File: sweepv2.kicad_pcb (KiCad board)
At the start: 2 copper layers, 216.9 x 86.6 mm, 50 parts, among them J1 AudioJack4dpb, J2 AudioJack4dpb, SW10 SW_Push, SW11 SW_Push, SW11_r1 SW_Push, SW12 SW_Push, SW12_r1 SW_Push, SW13_r1 SW_Push, SW14 SW_Push, SW15 SW_Push, SW15_r1 SW_Push, SW16 SW_Push, SW16_r1 SW_Push, SW17 SW_Push, SW17_r1 SW_Push, SW18 SW_Push, SW18_r1 SW_Push, SW2 SW_Push, SW20 SW_Push, SW20_r1 SW_Push, SW21 SW_Push, SW21_r1 SW_Push, SW2_r1 SW_Push, SW3 SW_Push, SW3_r1 SW_Push, SW4 SW_Push, SW4_r1 SW_Push, SW5 SW_Push, SW5_r1 SW_Push, SW6 SW_Push, SW6_r1 SW_Push, SW7_r1 SW_Push, SW8 SW_Push, SW8_r1 SW_Push, SW9 SW_Push, SW9_r1 SW_Push, U1 ProMicro-kbd, U2 ProMicro-kbd

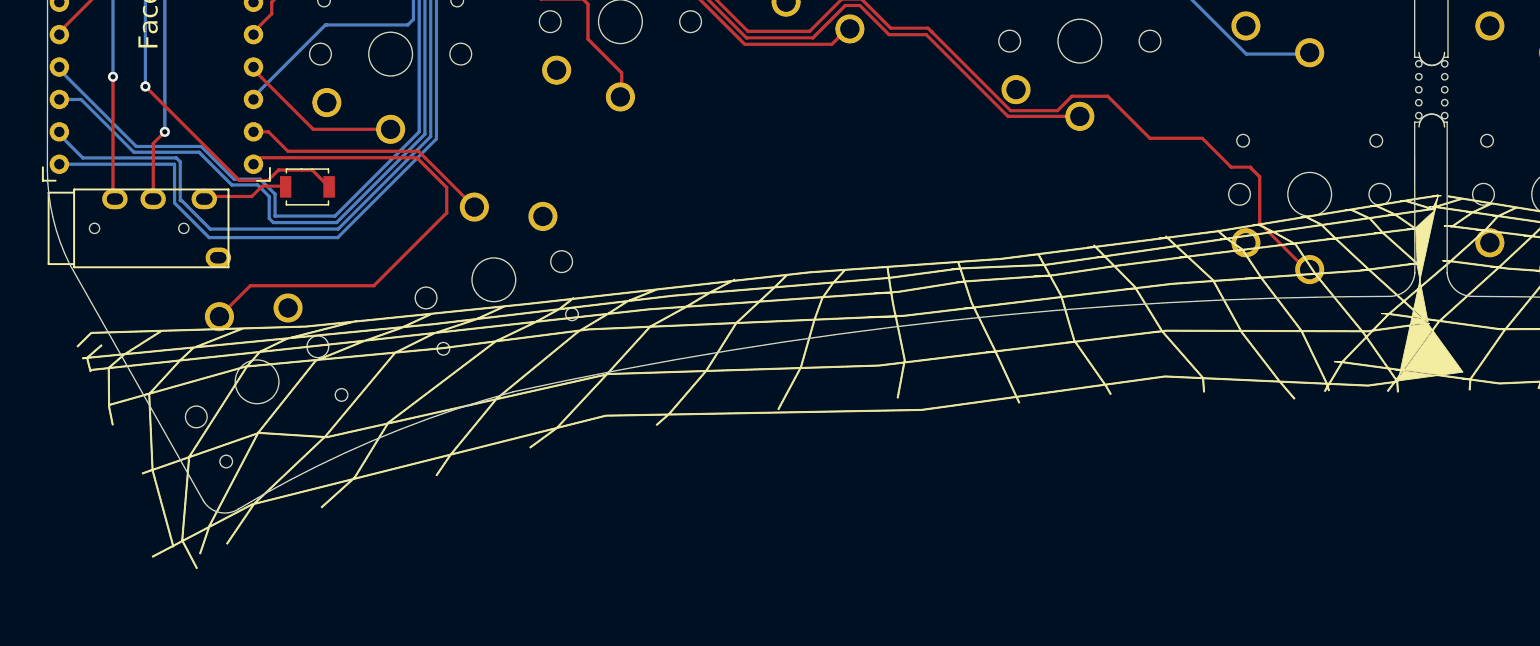
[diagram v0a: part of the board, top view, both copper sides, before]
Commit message: Add basic logos to board
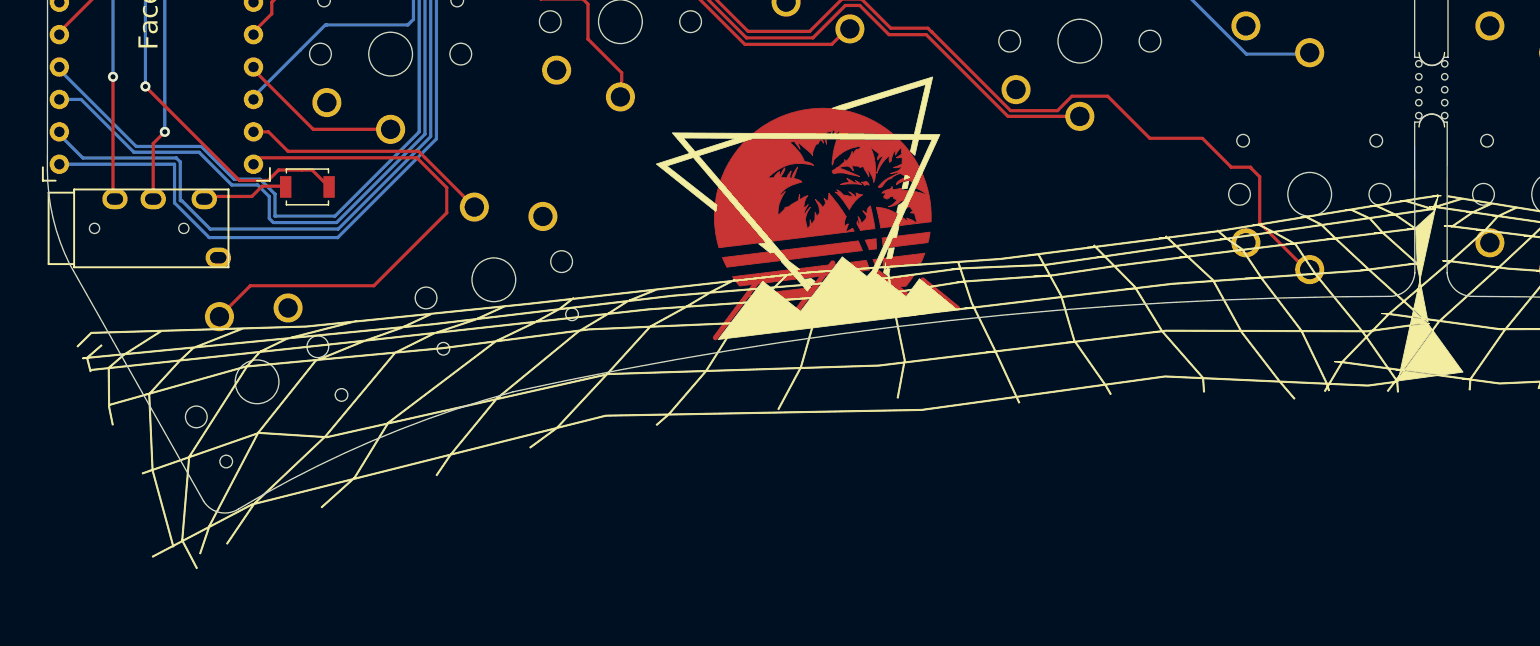
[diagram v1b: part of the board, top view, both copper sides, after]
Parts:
- added G***: LOGO, Kailh:ferris_broom, F.Cu at (82.7, 85.2)
- added G***: LOGO, Library:ferris_broom, F.Cu at (176.3, 83.2)
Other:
- board text removed: "Sweep v 2.2"

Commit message: Remove B logo footprint
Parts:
- removed the G*** at (176.3, 83.2)
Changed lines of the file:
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@@
     )
-  )
-  (footprint "Library:ferris_broom" (layer "F.Cu")
-    (at 176.291396 83.226564)
-    (attr board_only exclude_from_pos_files exclude_from_bom)
-    (fp_text reference "G***" (at 0 0) (layer "F.SilkS") hide
-      (effects (font (size 1.524 1.524) (thickness 0.3)))
-    )
-    (fp_text value "LOGO" (at 0.75 0) (layer "F.SilkS") hide
-      (effects (font (size 1.524 1.524) (thickness 0.3)))
-    )
-    (fp_poly (pts
-        (xy 0.893703 -2.398889)
-        (xy -0.517408 -2.398889)
-        (xy -0.517408 -4.515556)
-        (xy 0.893703 -4.515556)
-      ) (layer "F.Mask") (width 0) (fill solid))
-    (fp_poly (pts
-        (xy 0.893703 2.257777)
-        (xy -0.517408 2.257777)
-        (xy -0.517408 -0.117593)
-        (xy 0.893703 -0.117593)
-      ) (layer "F.Mask") (width 0) (fill solid))
-    (fp_poly (pts
-        (xy 3.786688 -7.190788)
-        (xy 5.46311 -5.844352)
-        (xy 5.446596 -4.374445)
-        (xy 5.430083 -2.904538)
-        (xy 5.324688 -2.516482)
-        (xy 5.289097 -2.385703)
-        (xy 5.257136 -2.268751)
-        (xy 5.231118 -2.174053)
-        (xy 5.213356 -2.110036)
-        (xy 5.206857 -2.087269)
-        (xy 5.205831 -2.062536)
-        (xy 5.228913 -2.050199)
-        (xy 5.286103 -2.046256)
-        (xy 5.309736 -2.046112)
-        (xy 5.425049 -2.046112)
-        (xy 5.440654 -0.405695)
-        (xy 5.443421 -0.100554)
-        (xy 5.446033 0.214915)
-        (xy 5.448444 0.533626)
-        (xy 5.450612 0.848493)
-        (xy 5.452493 1.152429)
-        (xy 5.454044 1.438347)
-        (xy 5.45522 1.699161)
-        (xy 5.455978 1.927785)
-        (xy 5.456275 2.117131)
-        (xy 5.456277 2.132757)
-        (xy 5.456296 3.030792)
-        (xy 4.947144 4.856574)
-        (xy 3.843525 5.950021)
-        (xy 3.63503 6.156573)
-        (xy 3.421343 6.368225)
-        (xy 3.207342 6.58015)
-        (xy 2.997905 6.787519)
-        (xy 2.797908 6.985504)
-        (xy 2.612229 7.169278)
-        (xy 2.445745 7.334011)
-        (xy 2.303333 7.474875)
-        (xy 2.198335 7.578678)
-        (xy 1.656763 8.113888)
-        (xy -5.550371 8.113888)
-        (xy -5.550739 5.479814)
-        (xy -4.209815 5.479814)
-        (xy 1.804569 5.479814)
-        (xy 3.222638 4.086754)
-        (xy 4.640706 2.693694)
-        (xy 4.625192 1.446801)
-        (xy 4.622042 1.179152)
-        (xy 4.619107 0.901534)
-        (xy 4.61645 0.622191)
-        (xy 4.614138 0.349365)
-        (xy 4.612237 0.091297)
-        (xy 4.610812 -0.143769)
-        (xy 4.60993 -0.34759)
-        (xy 4.609653 -0.499769)
-        (xy 4.609629 -1.199445)
-        (xy 3.586574 -1.199445)
-        (xy 3.349896 -1.199927)
-        (xy 3.137497 -1.201324)
-        (xy 2.952981 -1.20356)
-        (xy 2.79995 -1.206558)
-        (xy 2.682011 -1.210243)
-        (xy 2.602766 -1.214538)
-        (xy 2.565819 -1.219369)
-        (xy 2.563518 -1.220984)
-        (xy 2.579817 -1.240902)
-        (xy 2.626794 -1.290877)
-        (xy 2.701569 -1.368005)
-        (xy 2.801261 -1.469384)
-        (xy 2.922992 -1.592112)
-        (xy 3.06388 -1.733284)
-        (xy 3.221046 -1.889998)
-        (xy 3.39161 -2.059351)
-        (xy 3.572692 -2.238441)
-        (xy 3.584322 -2.24992)
-        (xy 4.605126 -3.257315)
-        (xy 4.619756 -4.350926)
-        (xy 4.634386 -5.444538)
-        (xy 3.21842 -6.579306)
-        (xy 1.802454 -7.714075)
-        (xy -4.209815 -7.714075)
-        (xy -4.209815 5.479814)
-        (xy -5.550739 5.479814)
-        (xy -5.551405 0.711435)
-        (xy -5.552438 -6.691019)
-        (xy -5.298581 -7.613875)
-        (xy -5.044723 -8.536732)
-        (xy -1.467228 -8.536977)
-        (xy 2.110266 -8.537223)
-      ) (layer "F.Mask") (width 0) (fill solid))
   )
   (footprint "Kailh:SPDT_C128955" (layer "B.Cu")

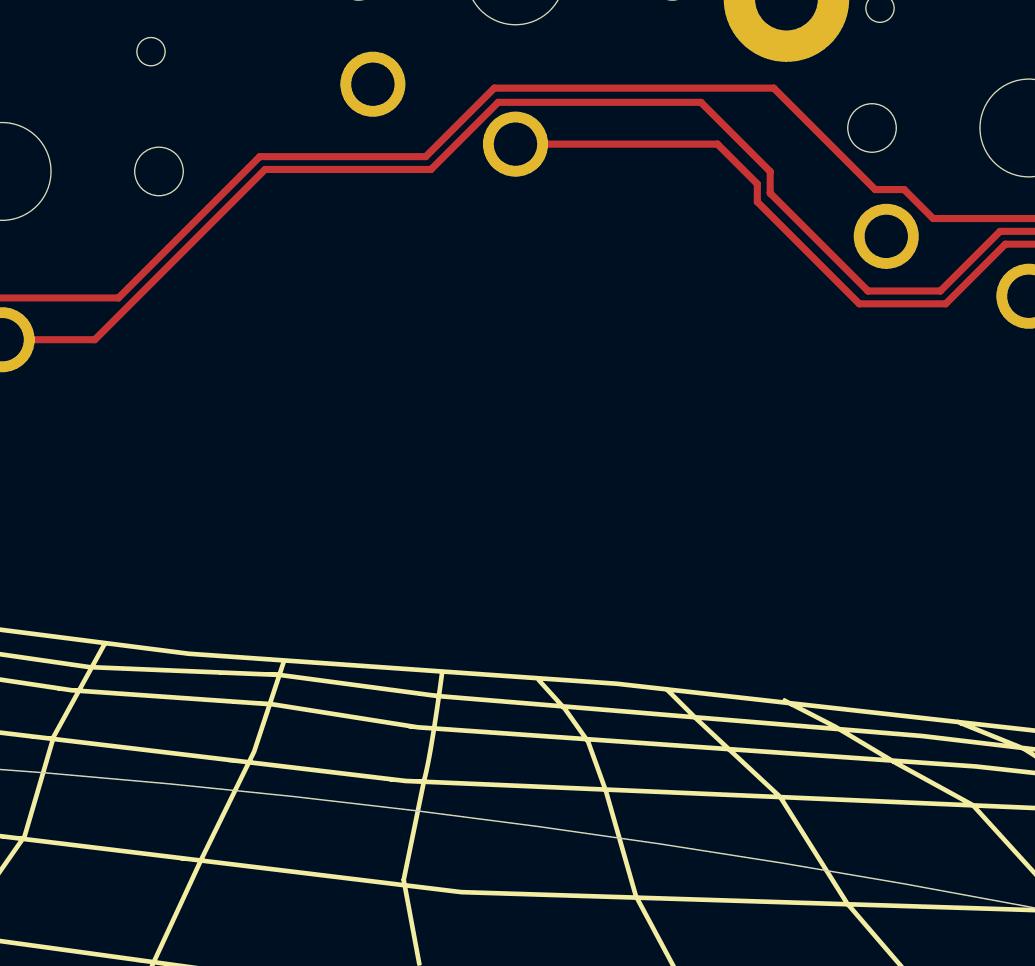
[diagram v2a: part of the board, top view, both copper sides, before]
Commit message: Add B logo with triangle
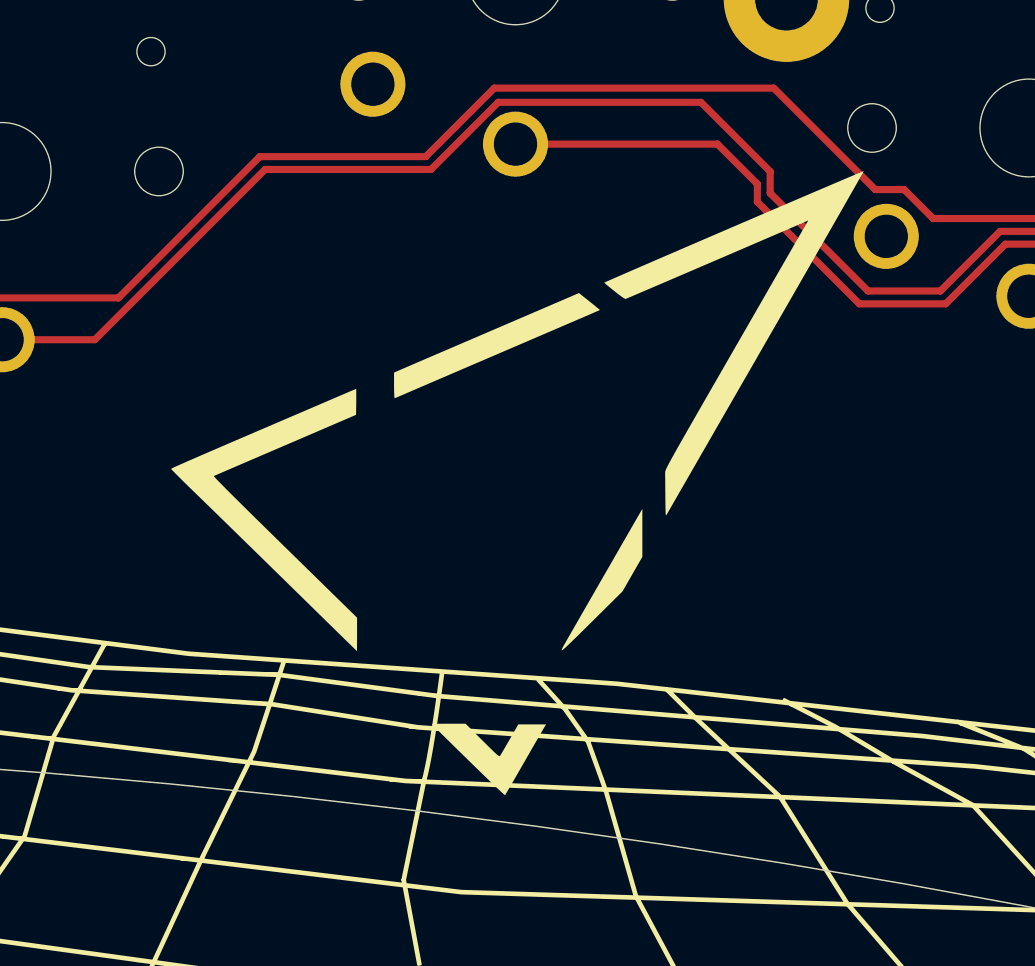
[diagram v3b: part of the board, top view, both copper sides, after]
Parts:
- added G***: LOGO, Library:silkscreen_triangle, F.Cu at (175.7, 82.8)

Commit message: Add gopher, rustacean and name
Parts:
- added G***: LOGO, Library:gopher, F.Cu at (192.8, 29.0)
- added G***: LOGO, Library:rustacean, F.Cu at (68.9, 26.7)
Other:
- board text added: "@b177y"
- board text added: "Ferris Sweep customised by @b177y"
- board text removed: "Sweep is based on the Ferris."
